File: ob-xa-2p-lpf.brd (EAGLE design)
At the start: 50.8 x 85.5 mm, 53 parts, among them IC1 AS3320, IC3 TL082P

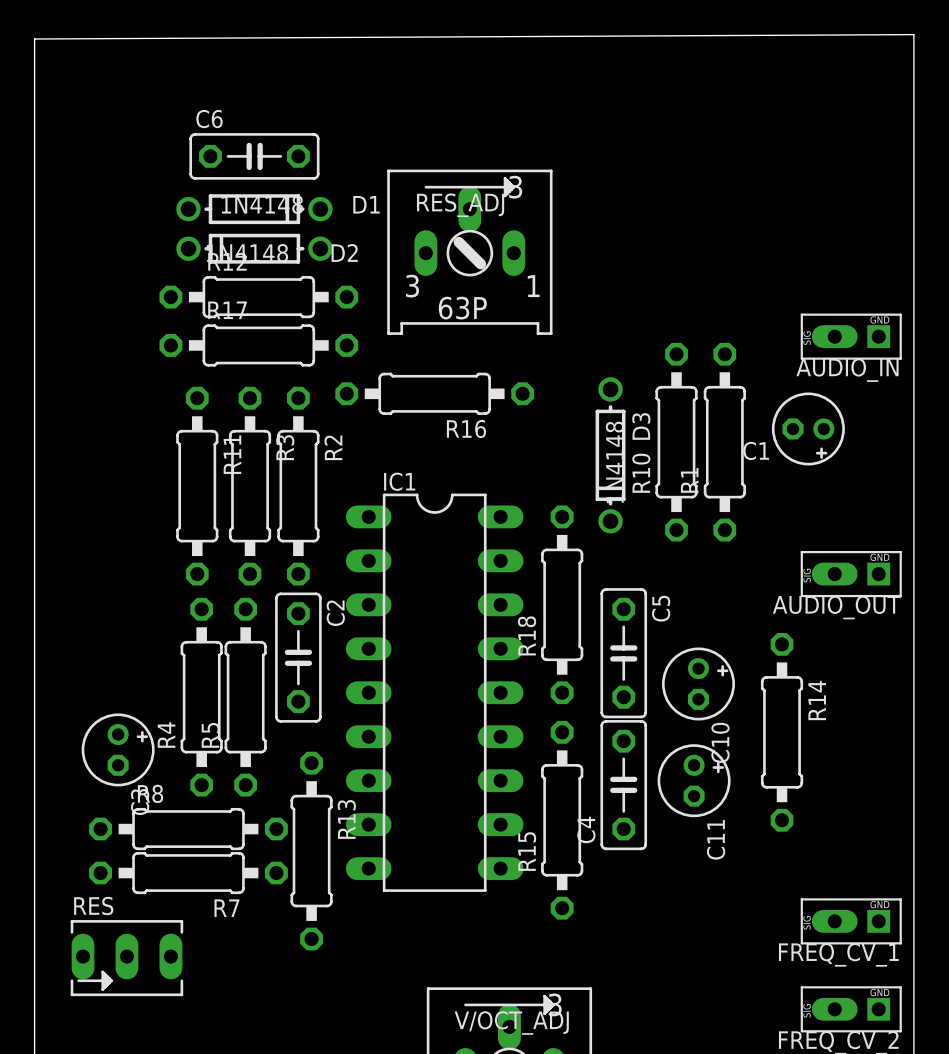
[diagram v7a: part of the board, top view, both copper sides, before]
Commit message: more layout cleanup
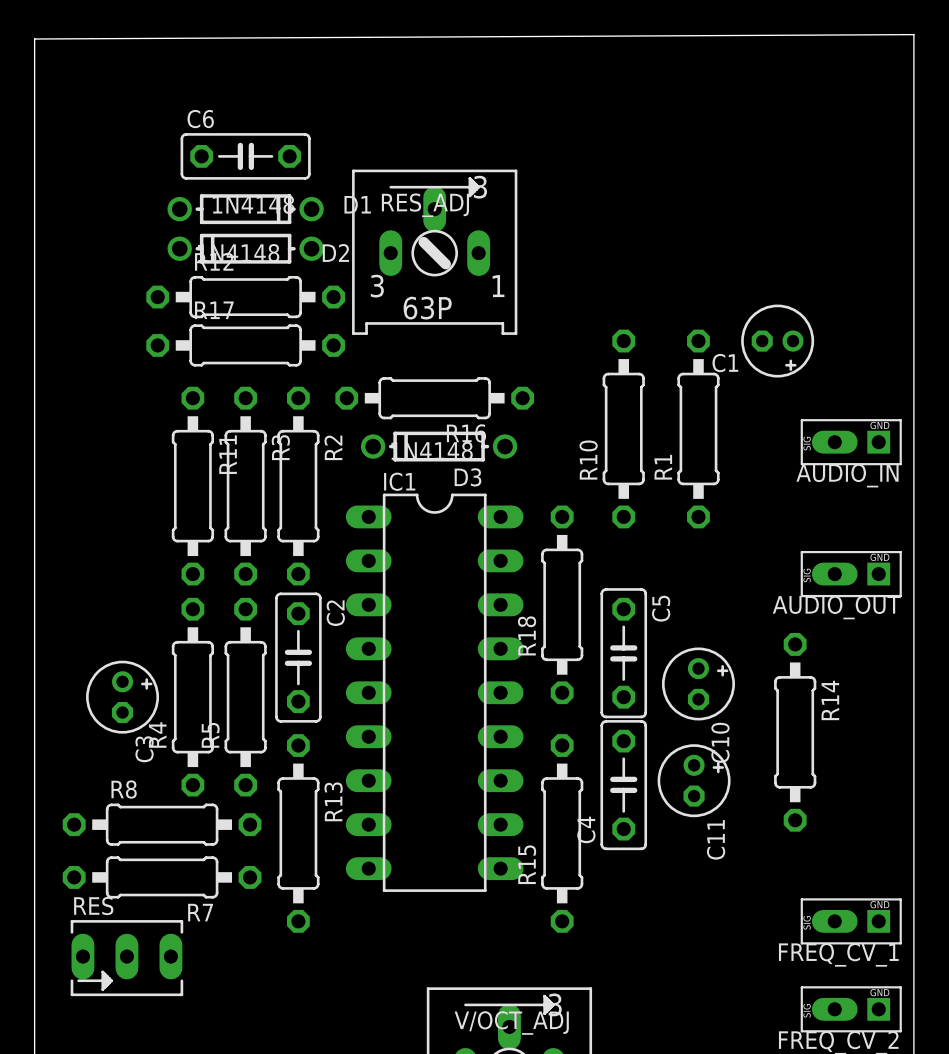
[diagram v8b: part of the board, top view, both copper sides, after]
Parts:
- moved D3 9.92 mm to (23.4, 61.7), turned to 180 degrees
- moved AUDIO_IN 6.10 mm to (47.5, 63.2)
- moved C1 5.38 mm to (42.9, 67.8)
- moved R10 3.14 mm to (34.0, 62.7)
- moved C3 3.06 mm to (5.08, 47.2)
- moved RES_ADJ 2.03 mm to (23.1, 72.9)
- moved R1 1.70 mm to (38.4, 62.7)
- moved R7 1.55 mm to (7.37, 36.8)
- moved R8 1.55 mm to (7.37, 39.9)
- moved R13 1.27 mm to (15.2, 39.4)
- moved R12 0.76 mm to (12.2, 70.4)
- moved R14 0.76 mm to (43.9, 45.2)
- moved R15 0.76 mm to (30.5, 39.4)
- moved R17 0.76 mm to (12.2, 67.6)
- moved C6 0.51 mm to (12.2, 78.5)
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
